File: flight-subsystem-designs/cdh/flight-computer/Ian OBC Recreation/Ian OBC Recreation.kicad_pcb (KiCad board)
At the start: 4 copper layers, 90 x 96 mm, 38 parts, among them J8 Conn_02x26_Odd_Even, Q1 AON6411, Q2 AON6411, U1 BEAGLEBONEBLACK, U2 TPS2400DBVR, U3 TCAN337G, U4 MCP7940N-xSN, U5 ADM3485EARZ, U6 MAX706RESA+T, U7 TMP36xS, U8 TPS2400DBVR

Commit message: Librecube Friendly Hopefully; Wiring Needs Work :C
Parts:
- removed J8: Conn_02x26_Odd_Even, Footprints:LibreCube_PC104_4x26_P2.54mm_adjacent
- added H1: MountingHole_Pad, MountingHole:MountingHole_3.2mm_M3_Pad_TopBottom, F.Cu at (147.0, 64.8)
- added H2: MountingHole_Pad, MountingHole:MountingHole_3.2mm_M3_Pad_TopBottom, F.Cu at (73.4, 64.8)
- added H3: MountingHole_Pad, MountingHole:MountingHole_3.2mm_M3_Pad_TopBottom, F.Cu at (149.7, 150.6)
- added H4: MountingHole_Pad, MountingHole:MountingHole_3.2mm_M3_Pad_TopBottom, F.Cu at (69.5, 150.6)
- added H5: PC/104 Connector, Connector_PinSocket_2.54mm:PinSocket_2x26_P2.54mm_Vertical, F.Cu at (78.4, 69.9)
- added H6: PC/104 Connector, Connector_PinSocket_2.54mm:PinSocket_2x26_P2.54mm_Vertical, F.Cu at (78.4, 64.8)
- moved U3 22.5 mm to (124.1, 132.4)
- moved C10 22.5 mm to (144.2, 132.8)
- moved C11 22.5 mm to (150.7, 133.5)
- moved R10 22.5 mm to (144.2, 134.8)
- moved R3 22.5 mm to (150.7, 131.5)
- moved TP5 22.5 mm to (143.6, 150.4)
- moved U7 22.5 mm to (138.4, 133.2)
- moved U8 22.5 mm to (146.0, 141.2)
- moved XTAL1 22.5 mm to (99.4, 137.2)
- moved BT1 22.5 mm to (109.0, 103.0)
- moved C1 22.5 mm to (127.2, 132.5)
- moved C2 22.5 mm to (121.0, 132.5)
- moved C3 22.5 mm to (124.0, 135.5)
- moved C4 22.5 mm to (111.7, 141.2)
- moved C5 22.5 mm to (127.2, 136.5)
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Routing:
- net /UART_RX: track 232.9 -> 96.6 mm, vias 1 -> 3
- net VDD_3V3B: track 38.8 -> 131.3 mm, vias 13 -> 16
- net /GPIO2_11: track 19.2 -> 65.9 mm
- net /GPIO1_15: track 57.3 -> 12.1 mm, vias 1 -> 0
- net /3V3IN: track 117.1 -> 156.3 mm
- net /CANL: track 86.1 -> 119.8 mm, vias 2 -> 8
- net /GPIO2_24: track 50.8 -> 20.7 mm, vias 2 -> 0
- net /CANH: track 86.1 -> 111.3 mm, vias 0 -> 6
- net /RS45B: track 125.0 -> 100.5 mm, vias 0 -> 4
- net /GPIO2_22: track 50.4 -> 27.4 mm, vias 0 -> 1
- net /SYSRST: track 86.0 -> 102.3 mm
- net /I2C_SCL: track 111.2 -> 123.3 mm, vias 5 -> 2
- net /GPIO2_9: track 44.2 -> 34.1 mm, vias 0 -> 1
- net /GPIO2_1: track 29.1 -> 37.9 mm
- net /GPIO1_14: track 23.5 -> 14.9 mm, vias 1 -> 0
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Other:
- board size 90 x 96 mm -> 90.3 x 95.9 mm

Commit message: feat improvement
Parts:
- removed Q1, Q2: AON6411, Package_DFN_QFN:AO_DFN-8-1EP_5.55x5.2mm_P1.27mm_EP4.12x4.6mm
- removed TP3, TP5: TestPoint, TestPoint:TestPoint_THTPad_D3.0mm_Drill1.5mm
- removed U2, U8: TPS2400DBVR, Footprints:SOT95P280X145-5N
- added C12: 10 uF, Capacitor_SMD:C_0805_2012Metric_Pad1.18x1.45mm_HandSolder, F.Cu at (117.8, 149.3)
- added C7: 100 nF, Capacitor_SMD:C_0805_2012Metric_Pad1.18x1.45mm_HandSolder, F.Cu at (108.8, 149.3)
- added C8: 100 nF, Capacitor_SMD:C_0805_2012Metric_Pad1.18x1.45mm_HandSolder, F.Cu at (111.8, 149.3)
- added C9: 10 uF, Capacitor_SMD:C_0805_2012Metric_Pad1.18x1.45mm_HandSolder, F.Cu at (114.8, 149.3)
- added D1: BAT54CW, Package_TO_SOT_SMD:SOT-323_SC-70, F.Cu at (96.7, 147.1)
- moved R7 9.32 mm to (130.0, 132.4), turned to -90 degrees
- moved R6 6.76 mm to (128.0, 132.5), turned to 90 degrees
- moved C1 6.05 mm to (124.0, 137.6), turned to 0 degrees
- moved C5 1.96 mm to (128.9, 135.5), turned to 180 degrees
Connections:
- H5 pad 14: /SYSRST -> /PPS
- H6 pad 25: /5VIN -> SYS_5V
- H6 pad 27: /3V3IN -> VDD_3V3B
- U1 pad P8_3: unconnected-(U1-GPIO1_6-PadP8_3) -> /PPS
- U1 pad P9_19: unconnected-(U1-I2C2_SCL-PadP9_19) -> /DCAN1TX
- U1 pad P9_20: unconnected-(U1-I2C2_SDA-PadP9_20) -> /DCAN1RX
- U1 pad P9_24: /DCAN1RX -> unconnected-(U1-UART1_TXD-PadP9_24)
- U1 pad P9_26: /DCAN1TX -> unconnected-(U1-UART1_RXD-PadP9_26)
- XTAL1 pad 4: VDD_3V3B -> /OSCVDD
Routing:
- net /3V3IN: track 156.3 -> 0.00 mm
- net /5VIN: track 126.2 -> 0.00 mm, vias 4 -> 0
- net SYS_5V: track 82.4 -> 180.9 mm, vias 2 -> 3
- net VDD_3V3B: track 131.3 -> 33.1 mm, vias 16 -> 10
- net /SYSRST: track 102.3 -> 11.8 mm, vias 2 -> 1
- net /GPIO3_20: track 87.5 -> 59.6 mm, vias 0 -> 2
- net Net-(BT1-+): track 59.2 -> 81.9 mm, vias 1 -> 3
- net /UART_TX: track 141.6 -> 128.7 mm
- net /OSCVDD: track 0.00 -> 12.7 mm, vias 0 -> 2
- net Net-(Q2-G): track 11.6 -> 0.00 mm, vias 2 -> 0
- net /CANH: track 111.3 -> 100.4 mm, vias 6 -> 4
- net Net-(Q1-G): track 10.8 -> 0.00 mm
- net /PPS: track 0.00 -> 10.0 mm
- net /DCAN1TX: track 6.31 -> 16.2 mm
- net /CANL: track 119.8 -> 110.9 mm, vias 8 -> 6
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
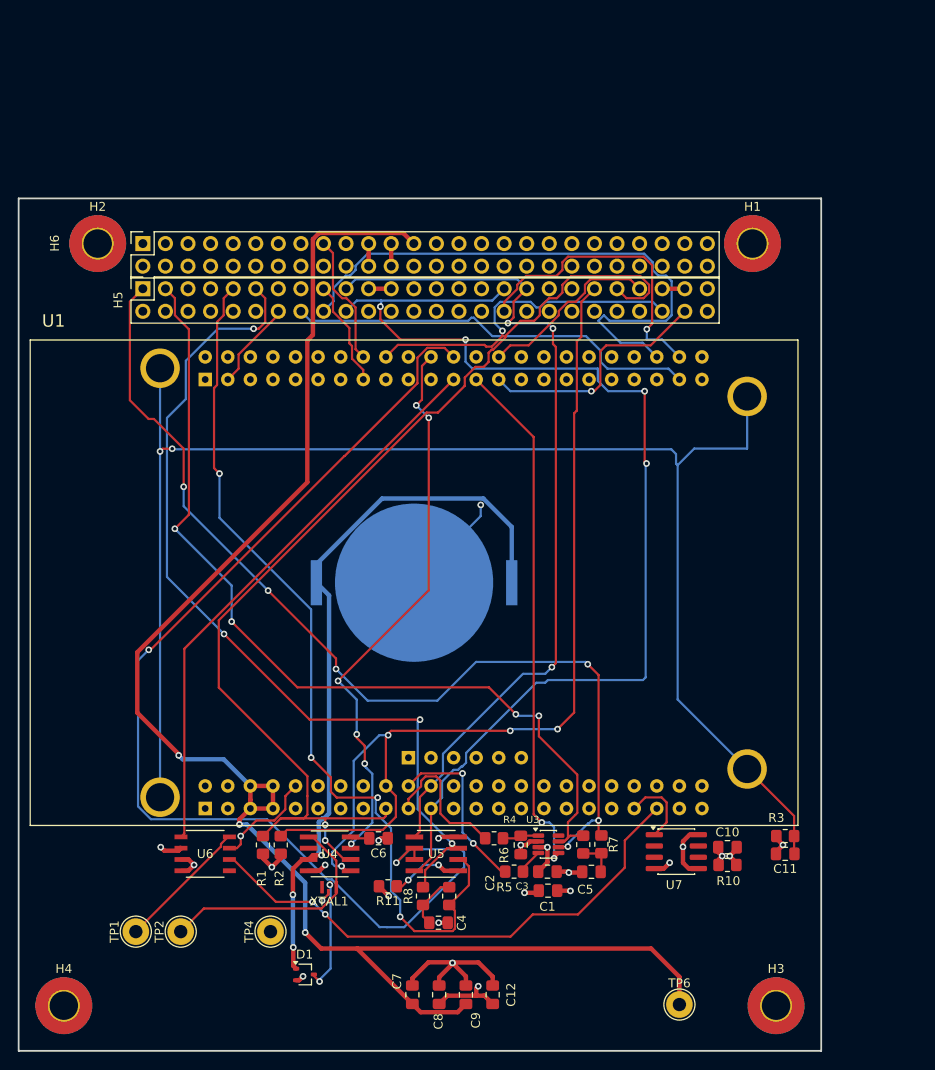
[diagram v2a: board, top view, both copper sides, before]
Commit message: Updated to match current ICD on Drive
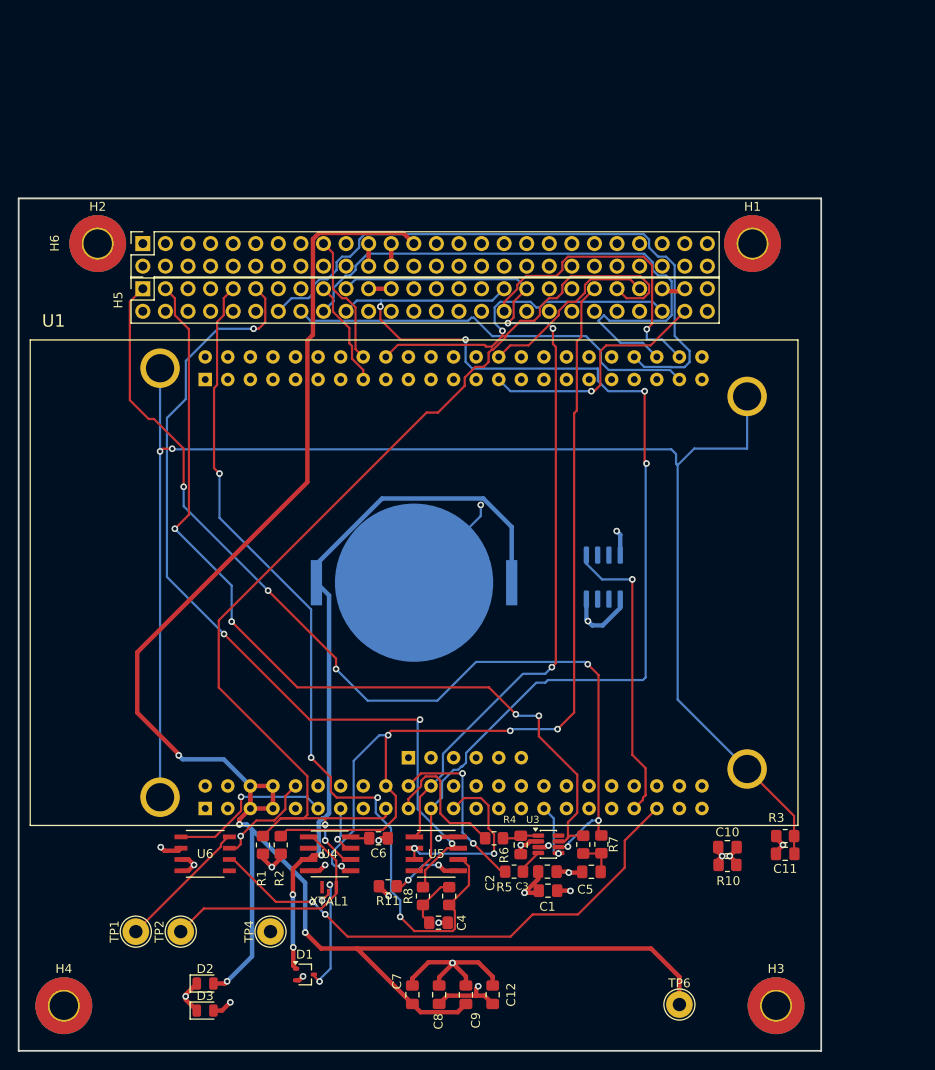
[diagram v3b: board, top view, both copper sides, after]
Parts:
- added D2: 5V, LED_SMD:LED_0805_2012Metric, F.Cu at (85.4, 148.1)
- added D3: 3V3, LED_SMD:LED_0805_2012Metric, F.Cu at (85.4, 151.1)
- U7: moved to B.Cu
- moved U7 32.0 mm to (130.2, 102.4), turned to -90 degrees
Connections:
- U1 pad P8_22: /RTCC_MFP -> unconnected-(U1-GPIO1_5-PadP8_22)
- U1 pad P8_23: /MRV -> unconnected-(U1-GPIO1_4-PadP8_23)
- U1 pad P8_24: /GPIO1_1 -> unconnected-(U1-GPIO1_1-PadP8_24)
- U1 pad P8_25: /CAN_FAULT -> unconnected-(U1-GPIO1_0-PadP8_25)
- U1 pad P8_29: /NANDWPI -> unconnected-(U1-GPIO2_23-PadP8_29)
- U1 pad P8_3: /PPS -> unconnected-(U1-GPIO1_6-PadP8_3)
- U1 pad P8_30: /NAND_HOLD -> unconnected-(U1-GPIO2_25-PadP8_30)
- U1 pad P8_40: /SEL_MODE -> /PPS
- U1 pad P9_11: unconnected-(U1-UART4_RXD-PadP9_11) -> /MRV
- U1 pad P9_13: unconnected-(U1-UART4_TXD-PadP9_13) -> /RTCC_MFP
- U1 pad P9_23: unconnected-(U1-GPIO1_17-PadP9_23) -> /GPIO1_17
- U1 pad P9_31: unconnected-(U1-SPI1_SCLK-PadP9_31) -> /CAN_FAULT
- U5 pad 2: /GPIO1_1 -> /GPIO1_17
- U5 pad 3: /GPIO1_1 -> /GPIO1_17
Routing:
- net /GPIO1_1: track 127.7 -> 0.00 mm, vias 2 -> 0
- net /PPS: track 10.0 -> 70.2 mm
- net /RTCC_MFP: track 63.4 -> 5.49 mm, vias 6 -> 1
- net /CAN_FAULT: track 58.8 -> 6.01 mm, vias 2 -> 1
- net /MRV: track 64.2 -> 18.8 mm, vias 0 -> 1
- net /Temp: track 8.60 -> 33.8 mm, vias 0 -> 1
- net /GPIO1_17: track 0.00 -> 20.9 mm, vias 0 -> 2
- net SYS_5V: track 180.9 -> 200.7 mm, vias 3 -> 4
- net GND: track 54.9 -> 59.9 mm, vias 13 -> 14
- net VDD_3V3B: track 33.1 -> 37.2 mm, vias 10 -> 11

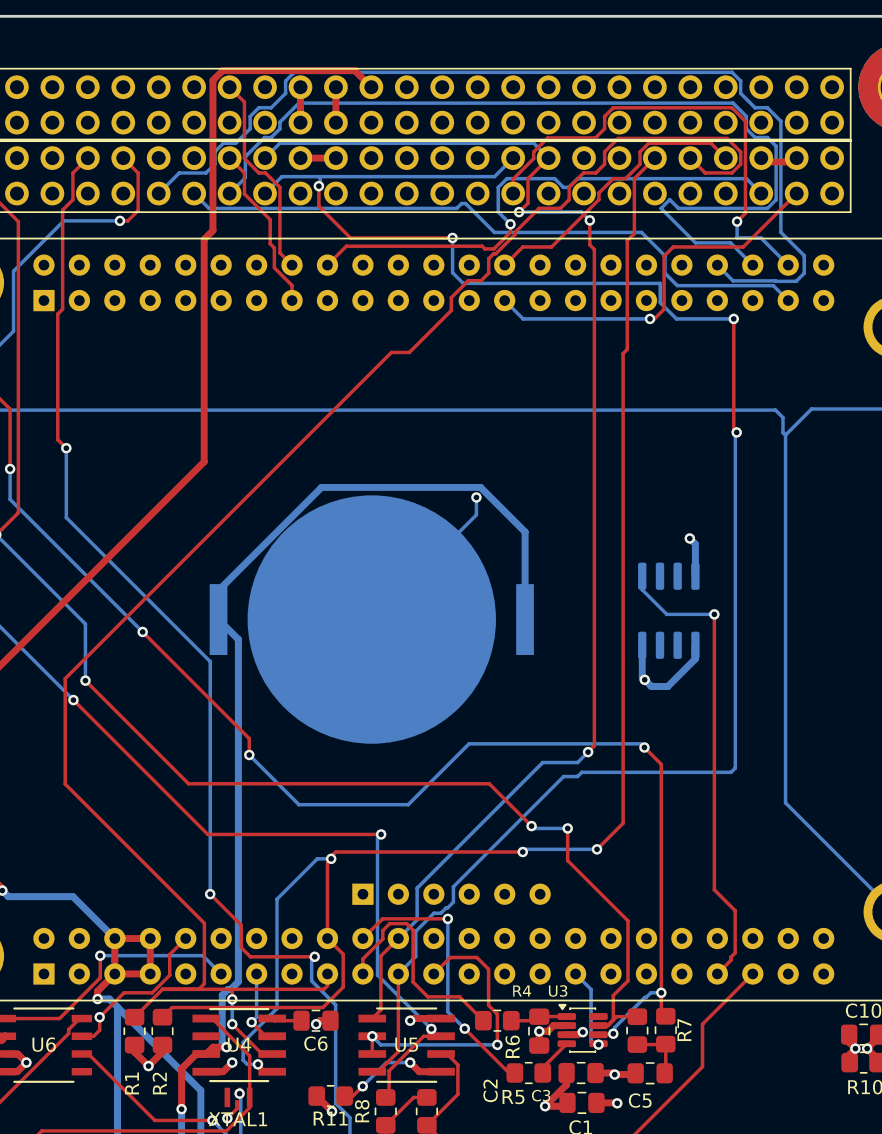
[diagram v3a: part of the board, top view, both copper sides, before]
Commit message: PCB side of schematic update to follow ICD
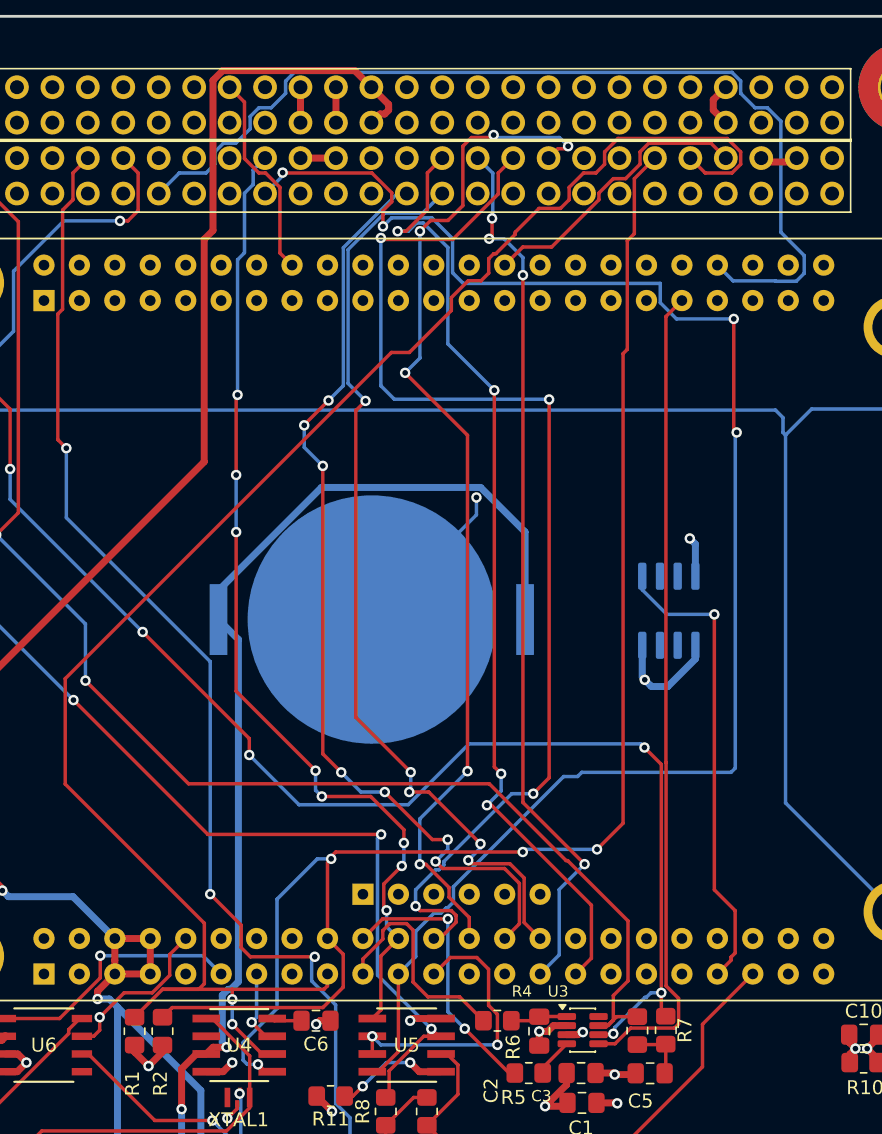
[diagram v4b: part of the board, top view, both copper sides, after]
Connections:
- H5 pad 10: GND -> unconnected-(H5-Pin_10-Pad10)
- H5 pad 12: GND -> unconnected-(H5-Pin_12-Pad12)
- H5 pad 13: /BATT_HEAT_EN -> unconnected-(H5-Pin_13-Pad13)
- H5 pad 15: /GPIO1_26 -> unconnected-(H5-Pin_15-Pad15)
- H5 pad 16: /GPIO2_8 -> unconnected-(H5-Pin_16-Pad16)
- H5 pad 17: /GPIO1_15 -> unconnected-(H5-Pin_17-Pad17)
- H5 pad 18: /GPIO2_11 -> unconnected-(H5-Pin_18-Pad18)
- H5 pad 22: /BATT_FAULT -> unconnected-(H5-Pin_22-Pad22)
- H5 pad 24: /CHRG -> unconnected-(H5-Pin_24-Pad24)
- H5 pad 25: /SWITCH_MODE_SEL -> unconnected-(H5-Pin_25-Pad25)
- H5 pad 26: /SOL_SHDN -> unconnected-(H5-Pin_26-Pad26)
- H5 pad 27: /3V3_S_EN -> unconnected-(H5-Pin_27-Pad27)
- H5 pad 28: /BURN1_N -> /SPI_CSO
- H5 pad 29: /BURN_IN -> /SPI_SCLK
- H5 pad 30: /BURN2_N -> /SPI_D1
- H5 pad 31: /5V_S_EN -> /SPI_DO
- H5 pad 33: /UART_TX -> /UART2_TX
- H5 pad 34: /GPIO2_9 -> GND
- H5 pad 35: /UART_RX -> /UART2_RX
- H5 pad 36: /GPIO1_27 -> GND
- H5 pad 46: /SWITCH_SHUTDOWN -> unconnected-(H5-Pin_46-Pad46)
- H5 pad 48: /GPIO2_1 -> unconnected-(H5-Pin_48-Pad48)
- H5 pad 50: /GPIO2_22 -> unconnected-(H5-Pin_50-Pad50)
- H5 pad 51: /SBWTDI0 -> unconnected-(H5-Pin_51-Pad51)
- H5 pad 52: /SBWTCK -> unconnected-(H5-Pin_52-Pad52)
- H5 pad 6: unconnected-(H5-Pin_6-Pad6) -> GND
- H6 pad 1: /BAT_BRD_TMP -> unconnected-(H6-Pin_1-Pad1)
- H6 pad 2: /PDU_TMP -> unconnected-(H6-Pin_2-Pad2)
- H6 pad 26: /5VIN -> SYS_5V
- H6 pad 28: /3V3IN -> VDD_3V3B
- H6 pad 31: GND -> unconnected-(H6-Pin_31-Pad31)
- H6 pad 32: GND -> unconnected-(H6-Pin_32-Pad32)
- H6 pad 4: unconnected-(H6-Pin_4-Pad4) -> GND
- H6 pad 45: unconnected-(H6-Pin_45-Pad45) -> /VBAT
- H6 pad 46: unconnected-(H6-Pin_46-Pad46) -> /VBAT
- H6 pad 6: unconnected-(H6-Pin_6-Pad6) -> GND
- U1 pad P8_37: unconnected-(U1-UART5_TXD-PadP8_37) -> /CAN_FAULT
- U1 pad P9_24: unconnected-(U1-UART1_TXD-PadP9_24) -> /UART2_TX
- U1 pad P9_26: unconnected-(U1-UART1_RXD-PadP9_26) -> /UART2_RX
- U1 pad P9_28: unconnected-(U1-SPI1_CS0-PadP9_28) -> /SPI_CSO
- U1 pad P9_29: unconnected-(U1-SPI1_D0-PadP9_29) -> /SPI_DO
- U1 pad P9_30: unconnected-(U1-SPI1_D1-PadP9_30) -> /SPI_D1
- U1 pad P9_31: /CAN_FAULT -> /SPI_SCLK
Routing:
- net /UART2_TX: track 0.00 -> 82.9 mm, vias 0 -> 4
- net /UART2_RX: track 0.00 -> 73.8 mm, vias 0 -> 6
- net /SPI_SCLK: track 0.00 -> 69.3 mm, vias 0 -> 4
- net /SPI_CSO: track 0.00 -> 68.6 mm, vias 0 -> 7
- net /SPI_D1: track 0.00 -> 67.7 mm, vias 0 -> 5
- net /GPIO2_11: track 65.9 -> 0.00 mm
- net /SPI_DO: track 0.00 -> 63.8 mm, vias 0 -> 4
- net /CAN_FAULT: track 6.01 -> 59.0 mm, vias 1 -> 0
- net /GPIO2_8: track 46.8 -> 0.00 mm
- net /GPIO2_1: track 37.9 -> 0.00 mm, vias 1 -> 0
- net /GPIO2_9: track 34.1 -> 0.00 mm, vias 1 -> 0
- net /GPIO2_22: track 27.4 -> 0.00 mm, vias 1 -> 0
- net /UART_RX: track 96.6 -> 71.4 mm, vias 3 -> 8
- net /UART_TX: track 128.7 -> 116.1 mm
- net /GPIO1_15: track 12.1 -> 0.00 mm
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
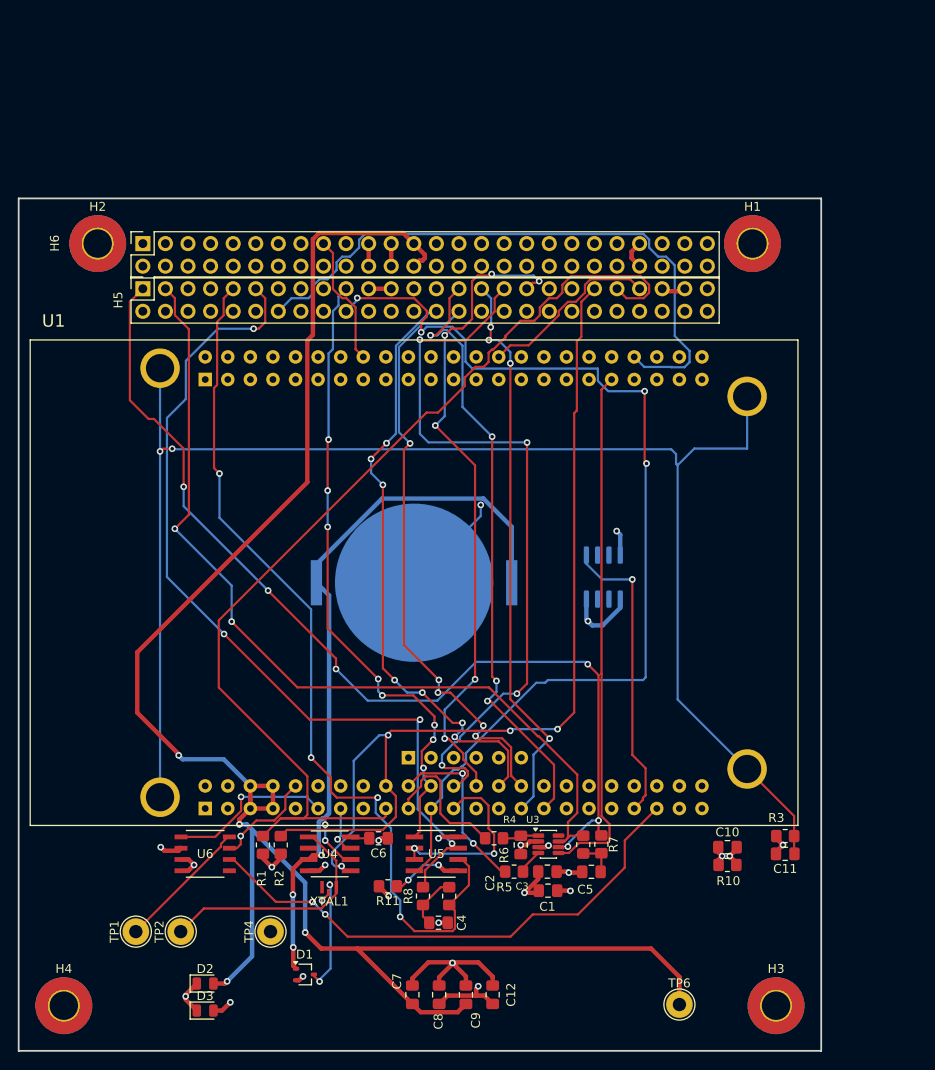
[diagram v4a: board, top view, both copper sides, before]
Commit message: New Board Version with better Signal Integrity
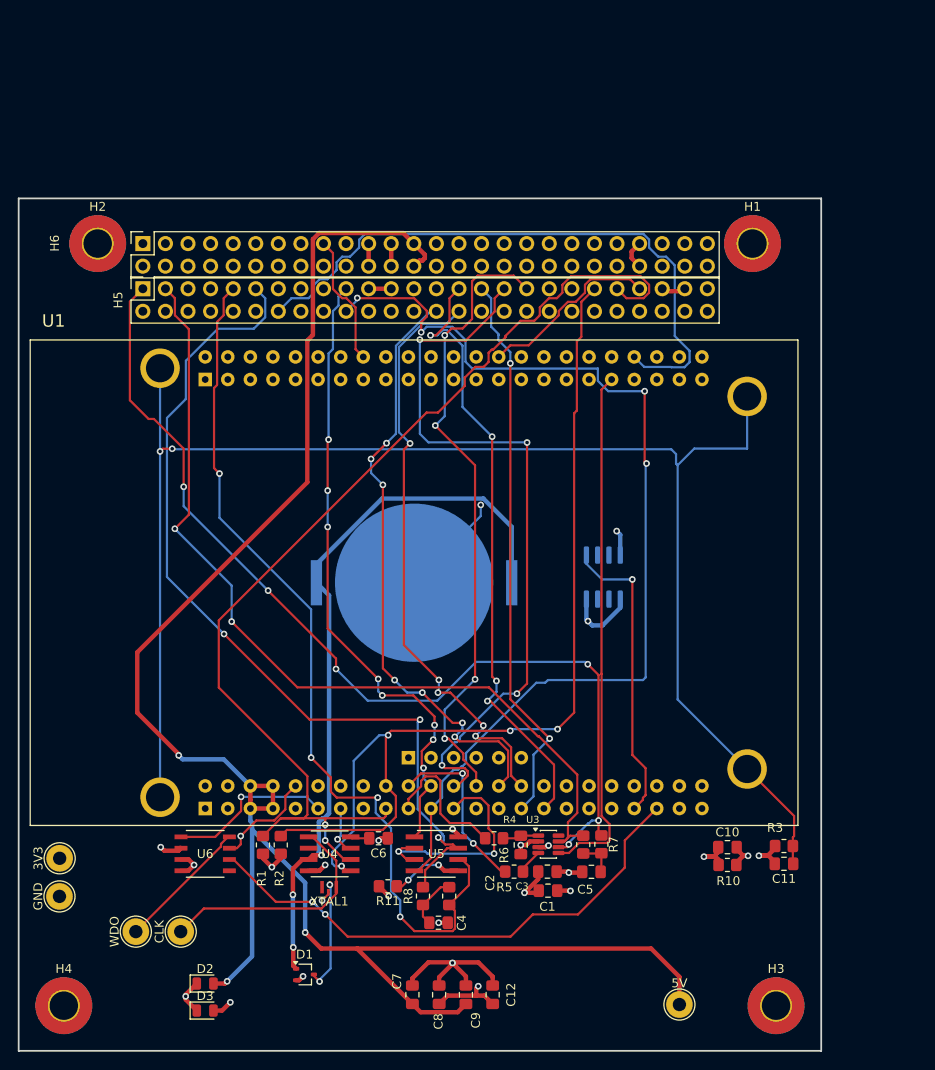
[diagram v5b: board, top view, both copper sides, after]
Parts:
- added GND: GND, TestPoint:TestPoint_THTPad_D3.0mm_Drill1.5mm, F.Cu at (69.1, 138.3)
- CLK: renamed from TP2; value TestPoint -> CLKOUT
- WDO: renamed from TP1; value TestPoint -> WDO
- moved 3V3 25.1 mm to (69.1, 134.0)
- moved C11 1.13 mm to (150.6, 134.6)
- moved R3 1.13 mm to (150.6, 132.6)
- renumbered TP4 to 3V3, TP6 to 5V
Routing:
- net /GPIO1_17: track 20.9 -> 25.4 mm
- net GND: track 59.9 -> 63.0 mm
- net /UART2_RX: track 73.8 -> 71.2 mm, vias 6 -> 4
- net /RS45B: track 98.6 -> 100.2 mm, vias 4 -> 3
- net SYS_5V: track 204.5 -> 203.0 mm, vias 4 -> 3
- net VDD_3V3B: track 37.2 -> 38.5 mm
- net Net-(C11-Pad1): track 171.6 -> 172.8 mm
- net /SPI_DO: track 63.8 -> 63.0 mm, vias 4 -> 2
